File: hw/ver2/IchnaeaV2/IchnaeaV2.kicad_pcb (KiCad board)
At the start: 4 copper layers, 100 x 100 mm, 7 parts, among them J1 Screw_Terminal_01x09, J2 Screw_Terminal_01x09, J3 Screw_Terminal_01x09

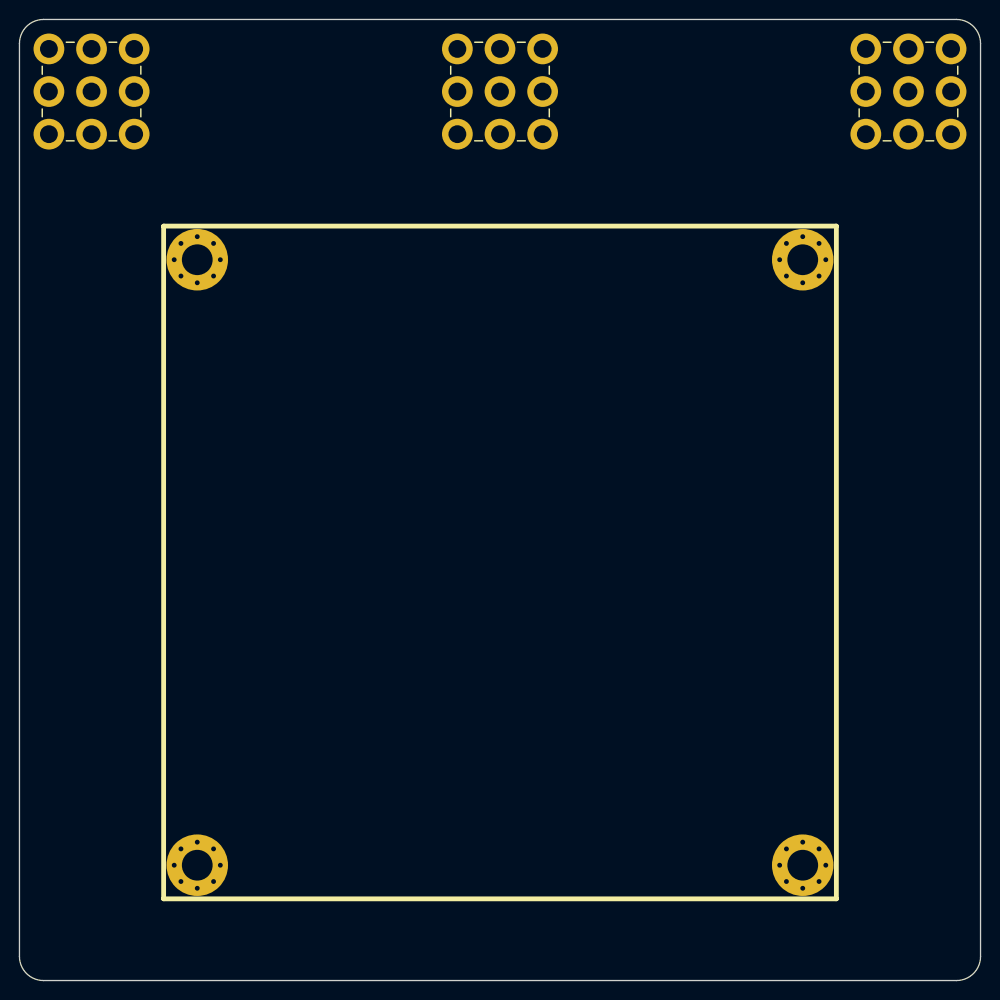
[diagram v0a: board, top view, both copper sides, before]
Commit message: Trying to optimize the high power loop area
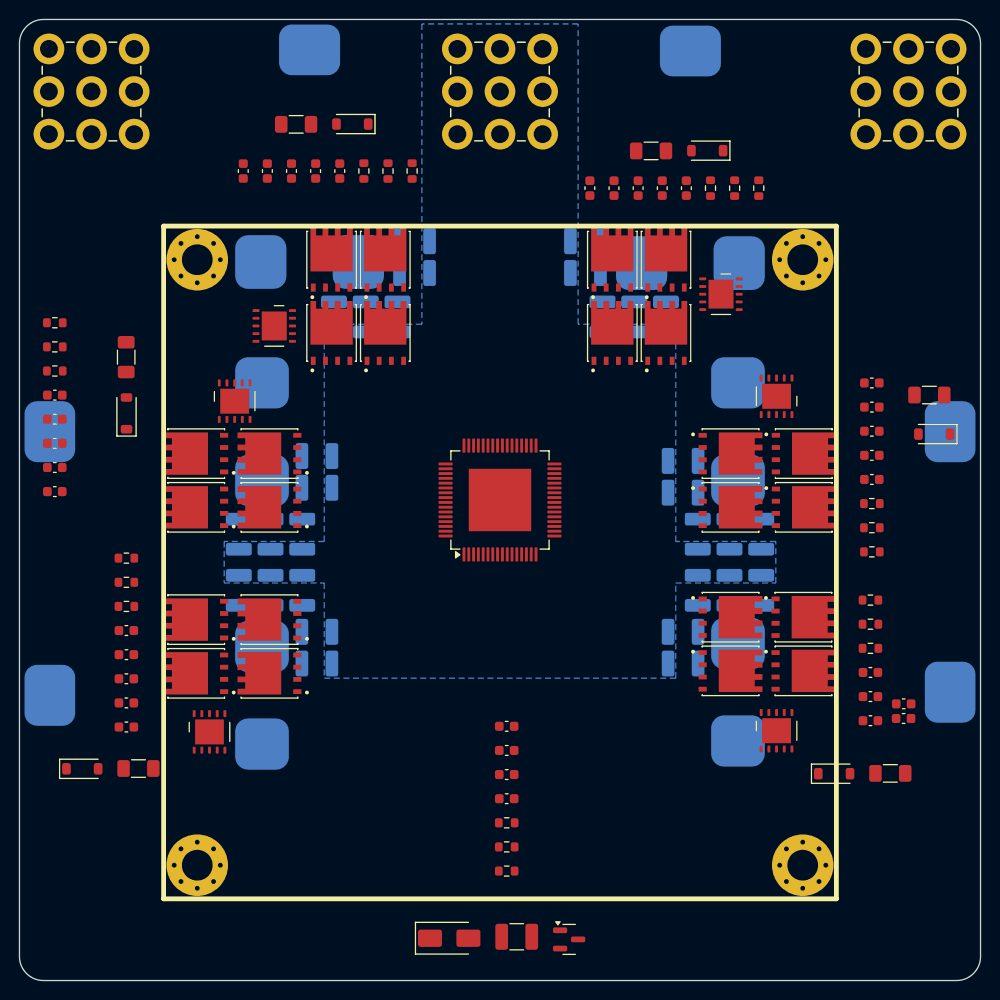
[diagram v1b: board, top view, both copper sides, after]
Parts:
- added C1: 10uF, Capacitor_SMD:C_0603_1608Metric, F.Cu at (145.7, 128.5)
- added C10: 470nF, Capacitor_SMD:C_0603_1608Metric, F.Cu at (183.5, 122.9)
- added C11: 10uF, Capacitor_SMD:C_1210_3225Metric_Pad1.33x2.70mm_HandSolder, B.Cu at (172.2, 114.4)
- added C12: 4.7uF, Capacitor_SMD:C_0603_1608Metric, F.Cu at (183.7, 92.8)
- added C13: 100nF, Capacitor_SMD:C_0603_1608Metric, F.Cu at (183.7, 95.3)
- added C14: 470nF, Capacitor_SMD:C_0603_1608Metric, F.Cu at (183.7, 97.8)
- added C15: 100nF, Capacitor_SMD:C_0603_1608Metric, F.Cu at (183.7, 100.4)
- added C16: 470nF, Capacitor_SMD:C_0603_1608Metric, F.Cu at (183.7, 102.9)
- added C17: 10uF, Capacitor_SMD:C_1210_3225Metric_Pad1.33x2.70mm_HandSolder, B.Cu at (172.2, 108.6)
- added C18: 4.7uF, Capacitor_SMD:C_0603_1608Metric, F.Cu at (154.4, 72.6)
- added C19: 100nF, Capacitor_SMD:C_0603_1608Metric, F.Cu at (156.9, 72.6)
- added C2: 100nF, Capacitor_SMD:C_0603_1608Metric, F.Cu at (145.7, 131.1)
- added C20: 470nF, Capacitor_SMD:C_0603_1608Metric, F.Cu at (159.4, 72.6)
- added C21: 100nF, Capacitor_SMD:C_0603_1608Metric, F.Cu at (161.9, 72.6)
- added C22: 470nF, Capacitor_SMD:C_0603_1608Metric, F.Cu at (164.4, 72.6)
- added C23: 10uF, Capacitor_SMD:C_1210_3225Metric_Pad1.33x2.70mm_HandSolder, B.Cu at (153.9, 78.1)
- added C24: 4.7uF, Capacitor_SMD:C_0603_1608Metric, F.Cu at (118.3, 70.8)
- added C25: 100nF, Capacitor_SMD:C_0603_1608Metric, F.Cu at (120.8, 70.8)
- added C26: 470nF, Capacitor_SMD:C_0603_1608Metric, F.Cu at (123.3, 70.8)
- added C27: 100nF, Capacitor_SMD:C_0603_1608Metric, F.Cu at (125.8, 70.8)
- added C28: 470nF, Capacitor_SMD:C_0603_1608Metric, F.Cu at (128.3, 70.8)
- added C29: 10uF, Capacitor_SMD:C_1210_3225Metric_Pad1.33x2.70mm_HandSolder, B.Cu at (136.1, 78.1)
- added C3: 10uF, Capacitor_SMD:C_0603_1608Metric, F.Cu at (145.7, 133.6)
- added C30: 4.7uF, Capacitor_SMD:C_0603_1608Metric, F.Cu at (98.7, 104.1)
- added C31: 100nF, Capacitor_SMD:C_0603_1608Metric, F.Cu at (98.7, 101.6)
- added C32: 470nF, Capacitor_SMD:C_0603_1608Metric, F.Cu at (98.7, 99.1)
- added C33: 100nF, Capacitor_SMD:C_0603_1608Metric, F.Cu at (98.7, 96.6)
- added C34: 470nF, Capacitor_SMD:C_0603_1608Metric, F.Cu at (98.7, 94.1)
- added C35: 10uF, Capacitor_SMD:C_1210_3225Metric_Pad1.33x2.70mm_HandSolder, B.Cu at (117.8, 108.6)
- added C36: 4.7uF, Capacitor_SMD:C_0603_1608Metric, F.Cu at (106.1, 128.6)
- added C37: 100nF, Capacitor_SMD:C_0603_1608Metric, F.Cu at (106.1, 126.1)
- added C38: 470nF, Capacitor_SMD:C_0603_1608Metric, F.Cu at (106.1, 123.6)
- added C39: 100nF, Capacitor_SMD:C_0603_1608Metric, F.Cu at (106.1, 121.1)
- added C4: 100nF, Capacitor_SMD:C_0603_1608Metric, F.Cu at (145.7, 136.1)
- added C40: 470nF, Capacitor_SMD:C_0603_1608Metric, F.Cu at (106.1, 118.6)
- added C41: 10uF, Capacitor_SMD:C_1210_3225Metric_Pad1.33x2.70mm_HandSolder, B.Cu at (121.1, 114.4)
- added C42: 10uF, Capacitor_SMD:C_1210_3225Metric_Pad1.33x2.70mm_HandSolder, B.Cu at (168.9, 114.4)
- added C43: 10uF, Capacitor_SMD:C_1210_3225Metric_Pad1.33x2.70mm_HandSolder, B.Cu at (168.9, 108.6)
- added C44: 10uF, Capacitor_SMD:C_1210_3225Metric_Pad1.33x2.70mm_HandSolder, B.Cu at (153.9, 81.4)
- added C45: 10uF, Capacitor_SMD:C_1210_3225Metric_Pad1.33x2.70mm_HandSolder, B.Cu at (131.0, 86.0)
- added C46: 10uF, Capacitor_SMD:C_1210_3225Metric_Pad1.33x2.70mm_HandSolder, B.Cu at (121.1, 108.6)
- added C47: 10uF, Capacitor_SMD:C_1210_3225Metric_Pad1.33x2.70mm_HandSolder, B.Cu at (124.4, 114.4)
- added C48: 10uF, Capacitor_SMD:C_1210_3225Metric_Pad1.33x2.70mm_HandSolder, B.Cu at (165.6, 114.4)
- added C49: 10uF, Capacitor_SMD:C_1210_3225Metric_Pad1.33x2.70mm_HandSolder, B.Cu at (165.6, 108.6)
- added C5: 10uF-75V, Capacitor_SMD:C_1210_3225Metric_Pad1.33x2.70mm_HandSolder, F.Cu at (146.7, 150.4)
- added C50: 10uF, Capacitor_SMD:C_1210_3225Metric_Pad1.33x2.70mm_HandSolder, B.Cu at (155.7, 86.0)
- added C51: 10uF, Capacitor_SMD:C_1210_3225Metric_Pad1.33x2.70mm_HandSolder, B.Cu at (134.3, 86.0)
- added C52: 10uF, Capacitor_SMD:C_1210_3225Metric_Pad1.33x2.70mm_HandSolder, B.Cu at (124.4, 108.6)
- added C53: 10uF, Capacitor_SMD:C_1210_3225Metric_Pad1.33x2.70mm_HandSolder, B.Cu at (126.0, 118.7)
- added C54: 10uF, Capacitor_SMD:C_1210_3225Metric_Pad1.33x2.70mm_HandSolder, B.Cu at (164.1, 118.7)
- added C55: 10uF, Capacitor_SMD:C_1210_3225Metric_Pad1.33x2.70mm_HandSolder, B.Cu at (164.1, 104.2)
- added C56: 10uF, Capacitor_SMD:C_1210_3225Metric_Pad1.33x2.70mm_HandSolder, B.Cu at (159.0, 86.0)
- added C57: 10uF, Capacitor_SMD:C_1210_3225Metric_Pad1.33x2.70mm_HandSolder, B.Cu at (127.7, 86.0)
- added C58: 10uF, Capacitor_SMD:C_1210_3225Metric_Pad1.33x2.70mm_HandSolder, B.Cu at (126.0, 103.7)
- added C59: 10uF, Capacitor_SMD:C_1210_3225Metric_Pad1.33x2.70mm_HandSolder, B.Cu at (126.0, 122.0)
- added C6: 4.7uF, Capacitor_SMD:C_0603_1608Metric, F.Cu at (187.0, 126.2)
- added C60: 10uF, Capacitor_SMD:C_1210_3225Metric_Pad1.33x2.70mm_HandSolder, B.Cu at (164.1, 122.0)
- added C61: 10uF, Capacitor_SMD:C_1210_3225Metric_Pad1.33x2.70mm_HandSolder, B.Cu at (164.1, 100.9)
- added C62: 10uF, Capacitor_SMD:C_1210_3225Metric_Pad1.33x2.70mm_HandSolder, B.Cu at (162.3, 86.0)
- added C63: 10uF, Capacitor_SMD:C_1210_3225Metric_Pad1.33x2.70mm_HandSolder, B.Cu at (136.1, 81.4)
- added C64: 10uF, Capacitor_SMD:C_1210_3225Metric_Pad1.33x2.70mm_HandSolder, B.Cu at (126.0, 100.4)
- added C65: 10uF, Capacitor_SMD:C_1210_3225Metric_Pad1.33x2.70mm_HandSolder, B.Cu at (117.8, 114.4)
- added C7: 100nF, Capacitor_SMD:C_0603_1608Metric, F.Cu at (187.0, 127.7)
- added C8: 470nF, Capacitor_SMD:C_0603_1608Metric, F.Cu at (183.5, 128.0)
- added C9: 100nF, Capacitor_SMD:C_0603_1608Metric, F.Cu at (183.5, 125.5)
- added D1: SS210, Diode_SMD:D_SMA, F.Cu at (139.7, 150.6)
- added D2: Z3V3, Diode_SMD:D_SOD-123, F.Cu at (179.8, 133.5)
- added D3: Z3V3, Diode_SMD:D_SOD-123, F.Cu at (190.2, 98.1)
- added D4: Z3V3, Diode_SMD:D_SOD-123, F.Cu at (166.6, 68.6)
- added D5: Z3V3, Diode_SMD:D_SOD-123, F.Cu at (129.6, 65.9)
- added D6: Z3V3, Diode_SMD:D_SOD-123, F.Cu at (106.1, 96.0)
- added D7: Z3V3, Diode_SMD:D_SOD-123, F.Cu at (101.5, 133.0)
- added L1: 4.7uH, Inductors:Bournes_L_PQ2614BLA, B.Cu at (184.1, 125.0)
- added L2: 4.7uH, Inductors:Bournes_L_PQ2614BLA, B.Cu at (184.1, 97.9)
- added L3: 4.7uH, Inductors:Bournes_L_PQ2614BLA, B.Cu at (164.8, 66.0)
- added L4: 4.7uH, Inductors:Bournes_L_PQ2614BLA, B.Cu at (125.2, 65.9)
- added L5: 4.7uH, Inductors:Bournes_L_PQ2614BLA, B.Cu at (105.9, 97.9)
- added L6: 4.7uH, Inductors:Bournes_L_PQ2614BLA, B.Cu at (105.9, 125.3)
- added Q1: BSS138, Package_TO_SOT_SMD:SOT-23, F.Cu at (152.2, 150.7)
- added Q10: MCAC80N10Y, Mosfets:TRANS_BSC076N06NS3-G, F.Cu at (156.7, 80.0)
- added Q11: MCAC80N10Y, Mosfets:TRANS_BSC076N06NS3-G, F.Cu at (162.3, 87.6)
- added Q12: MCAC80N10Y, Mosfets:TRANS_BSC076N06NS3-G, F.Cu at (162.3, 80.0)
- added Q13: MCAC80N10Y, Mosfets:TRANS_BSC076N06NS3-G, F.Cu at (156.7, 87.6)
- added Q14: MCAC80N10Y, Mosfets:TRANS_BSC076N06NS3-G, F.Cu at (133.1, 80.0)
- added Q15: MCAC80N10Y, Mosfets:TRANS_BSC076N06NS3-G, F.Cu at (127.5, 87.6)
- added Q16: MCAC80N10Y, Mosfets:TRANS_BSC076N06NS3-G, F.Cu at (127.5, 80.0)
- added Q17: MCAC80N10Y, Mosfets:TRANS_BSC076N06NS3-G, F.Cu at (133.1, 87.6)
- added Q18: MCAC80N10Y, Mosfets:TRANS_BSC076N06NS3-G, F.Cu at (113.4, 100.2)
- added Q19: MCAC80N10Y, Mosfets:TRANS_BSC076N06NS3-G, F.Cu at (121.0, 105.8)
- added Q2: MCAC80N10Y, Mosfets:TRANS_BSC076N06NS3-G, F.Cu at (176.6, 117.2)
- added Q20: MCAC80N10Y, Mosfets:TRANS_BSC076N06NS3-G, F.Cu at (113.4, 105.8)
- added Q21: MCAC80N10Y, Mosfets:TRANS_BSC076N06NS3-G, F.Cu at (121.0, 100.2)
- added Q22: MCAC80N10Y, Mosfets:TRANS_BSC076N06NS3-G, F.Cu at (113.4, 117.4)
- added Q23: MCAC80N10Y, Mosfets:TRANS_BSC076N06NS3-G, F.Cu at (121.0, 117.4)
- added Q24: MCAC80N10Y, Mosfets:TRANS_BSC076N06NS3-G, F.Cu at (113.4, 123.0)
- added Q25: MCAC80N10Y, Mosfets:TRANS_BSC076N06NS3-G, F.Cu at (121.0, 123.0)
- added Q3: MCAC80N10Y, Mosfets:TRANS_BSC076N06NS3-G, F.Cu at (169.0, 117.2)
- added Q4: MCAC80N10Y, Mosfets:TRANS_BSC076N06NS3-G, F.Cu at (176.6, 122.8)
- added Q5: MCAC80N10Y, Mosfets:TRANS_BSC076N06NS3-G, F.Cu at (169.0, 122.8)
- added Q6: MCAC80N10Y, Mosfets:TRANS_BSC076N06NS3-G, F.Cu at (176.6, 105.8)
- added Q7: MCAC80N10Y, Mosfets:TRANS_BSC076N06NS3-G, F.Cu at (169.0, 105.8)
- added Q8: MCAC80N10Y, Mosfets:TRANS_BSC076N06NS3-G, F.Cu at (176.6, 100.2)
- added Q9: MCAC80N10Y, Mosfets:TRANS_BSC076N06NS3-G, F.Cu at (169.0, 100.2)
- added R1: 1k, Resistor_SMD:R_0603_1608Metric, F.Cu at (145.7, 138.6)
- added R10: 6.2k-0.25w, Resistor_SMD:R_1206_3216Metric_Pad1.30x1.75mm_HandSolder, F.Cu at (189.7, 94.1)
- added R11: 6.2k, Resistor_SMD:R_0603_1608Metric, F.Cu at (183.7, 110.4)
- added R12: 2k, Resistor_SMD:R_0603_1608Metric, F.Cu at (166.9, 72.6)
- added R13: 47k, Resistor_SMD:R_0603_1608Metric, F.Cu at (169.4, 72.6)
- added R14: 6.2k-0.25w, Resistor_SMD:R_1206_3216Metric_Pad1.30x1.75mm_HandSolder, F.Cu at (160.7, 68.7)
- added R15: 6.2k, Resistor_SMD:R_0603_1608Metric, F.Cu at (171.9, 72.6)
- added R16: 2k, Resistor_SMD:R_0603_1608Metric, F.Cu at (130.8, 70.8)
- added R17: 47k, Resistor_SMD:R_0603_1608Metric, F.Cu at (133.3, 70.8)
- added R18: 6.2k-0.25w, Resistor_SMD:R_1206_3216Metric_Pad1.30x1.75mm_HandSolder, F.Cu at (123.8, 65.9)
- added R19: 6.2k, Resistor_SMD:R_0603_1608Metric, F.Cu at (135.9, 70.8)
- added R2: 10k, Resistor_SMD:R_0603_1608Metric, F.Cu at (145.7, 141.1)
- added R20: 2k, Resistor_SMD:R_0603_1608Metric, F.Cu at (98.7, 91.6)
- added R21: 47k, Resistor_SMD:R_0603_1608Metric, F.Cu at (98.7, 89.1)
- added R22: 6.2k-0.25w, Resistor_SMD:R_1206_3216Metric_Pad1.30x1.75mm_HandSolder, F.Cu at (106.1, 90.1)
- added R23: 6.2k, Resistor_SMD:R_0603_1608Metric, F.Cu at (98.7, 86.6)
- added R24: 2k, Resistor_SMD:R_0603_1608Metric, F.Cu at (106.1, 116.1)
- added R25: 47k, Resistor_SMD:R_0603_1608Metric, F.Cu at (106.1, 113.6)
- added R26: 6.2k-0.25w, Resistor_SMD:R_1206_3216Metric_Pad1.30x1.75mm_HandSolder, F.Cu at (107.4, 132.9)
- added R27: 6.2k, Resistor_SMD:R_0603_1608Metric, F.Cu at (106.1, 111.1)
- added R3: 100, Resistor_SMD:R_0603_1608Metric, F.Cu at (145.7, 143.6)
- added R4: 2k, Resistor_SMD:R_0603_1608Metric, F.Cu at (183.5, 120.4)
- added R5: 47k, Resistor_SMD:R_0603_1608Metric, F.Cu at (183.5, 117.9)
- added R6: 6.2k-0.25w, Resistor_SMD:R_1206_3216Metric_Pad1.30x1.75mm_HandSolder, F.Cu at (185.6, 133.4)
- added R7: 6.2k, Resistor_SMD:R_0603_1608Metric, F.Cu at (183.5, 115.4)
- added R8: 2k, Resistor_SMD:R_0603_1608Metric, F.Cu at (183.7, 105.4)
- added R9: 47k, Resistor_SMD:R_0603_1608Metric, F.Cu at (183.7, 107.9)
- added U1: LTC7871, Package_QFP:LQFP-64-1EP_10x10mm_P0.5mm_EP6.5x6.5mm, F.Cu at (145.0, 105.0)
- added U2: HIP2210, DFN:TDFN-10-1EP_4x4mm_P0.8mm_EP2.6x3mm, F.Cu at (173.8, 129.0)
- added U3: HIP2210, DFN:TDFN-10-1EP_4x4mm_P0.8mm_EP2.6x3mm, F.Cu at (173.8, 94.2)
- added U4: HIP2210, DFN:TDFN-10-1EP_4x4mm_P0.8mm_EP2.6x3mm, F.Cu at (168.0, 83.6)
- added U5: HIP2210, DFN:TDFN-10-1EP_4x4mm_P0.8mm_EP2.6x3mm, F.Cu at (121.5, 86.9)
- added U6: HIP2210, DFN:TDFN-10-1EP_4x4mm_P0.8mm_EP2.6x3mm, F.Cu at (117.4, 94.7)
- added U7: HIP2210, DFN:TDFN-10-1EP_4x4mm_P0.8mm_EP2.6x3mm, F.Cu at (114.8, 129.1)
- moved J2 42.5 mm to (183.1, 58.1)
- moved J3 42.5 mm to (140.6, 58.1)
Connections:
- J2 pad 1: GND -> +VLOW
- J2 pad 2: GND -> +VLOW
- J2 pad 3: GND -> +VLOW
- J2 pad 4: GND -> +VLOW
- J2 pad 5: GND -> +VLOW
- J2 pad 6: GND -> +VLOW
- J2 pad 7: GND -> +VLOW
- J2 pad 8: GND -> +VLOW
- J2 pad 9: GND -> +VLOW
- J3 pad 1: +VLOW -> GND
- J3 pad 2: +VLOW -> GND
- J3 pad 3: +VLOW -> GND
- J3 pad 4: +VLOW -> GND
- J3 pad 5: +VLOW -> GND
- J3 pad 6: +VLOW -> GND
- J3 pad 7: +VLOW -> GND
- J3 pad 8: +VLOW -> GND
- J3 pad 9: +VLOW -> GND
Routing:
- added copper zone on B.Cu, net GND
